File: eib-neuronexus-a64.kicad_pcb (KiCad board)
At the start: 2 copper layers, 53 x 59 mm, 5 parts, among them J1 xOLC-110-01-S-Q_1, J2 xOLC-110-01-S-Q_1, J3 Conn_02x35_Odd_Even, J4 Conn_01x02_Male

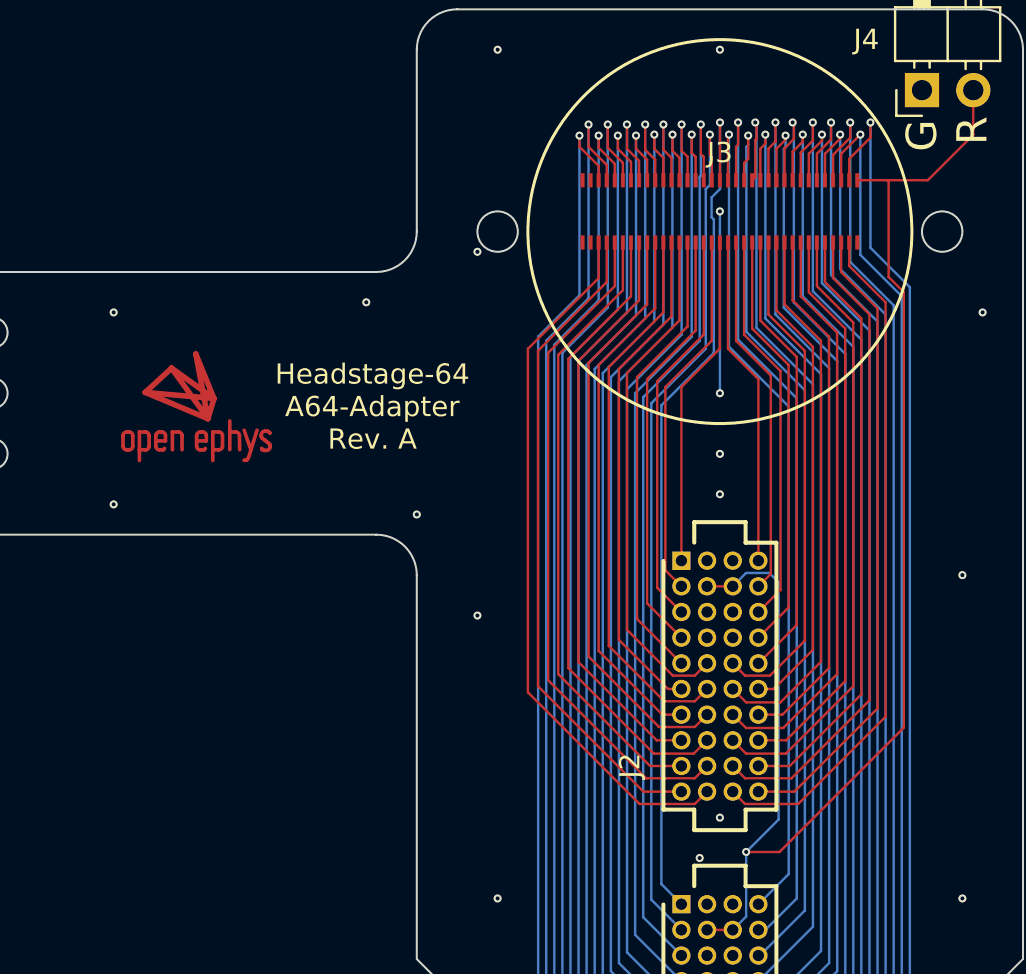
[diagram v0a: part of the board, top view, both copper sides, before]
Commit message: Revision B
- Fixed pinout to match 1.3B headstage-64
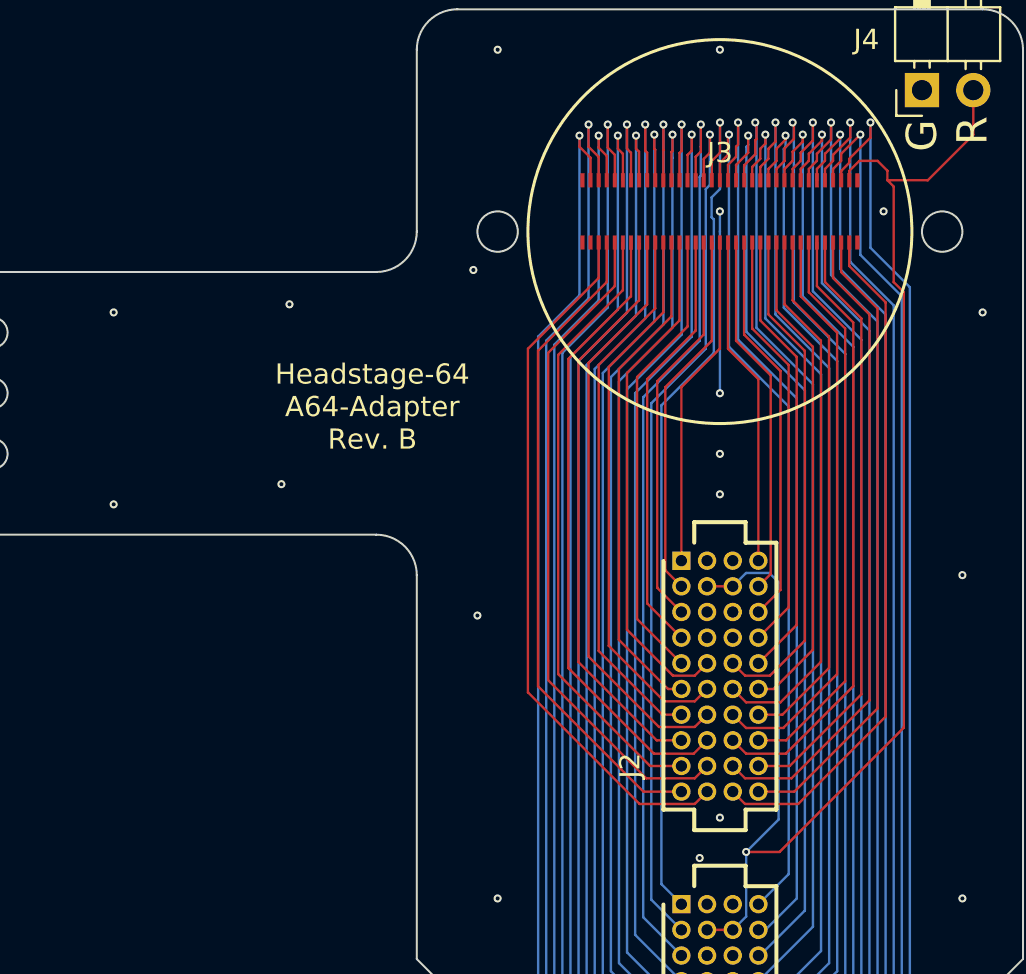
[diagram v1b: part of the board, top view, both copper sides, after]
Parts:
- removed ?: , jonnew-eagle:OE-LOGO-7X5
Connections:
- J3 pad 10: /Elec3 -> /Elec2
- J3 pad 12: /Elec4 -> /Elec3
- J3 pad 14: /Elec5 -> /Elec4
- J3 pad 16: /Elec6 -> /Elec5
- J3 pad 18: /Elec7 -> /Elec6
- J3 pad 2: /Ref -> GND
- J3 pad 20: /Elec8 -> /Elec7
- J3 pad 22: /Elec9 -> /Elec8
- J3 pad 24: /Elec10 -> /Elec9
- J3 pad 26: /Elec11 -> /Elec10
- J3 pad 28: /Elec12 -> /Elec11
- J3 pad 30: /Elec13 -> /Elec12
- J3 pad 32: /Elec14 -> /Elec13
- J3 pad 34: /Elec15 -> /Elec14
- J3 pad 36: /Elec48 -> /Elec15
- J3 pad 38: /Elec49 -> /Elec48
- J3 pad 4: /Elec0 -> /Ref
- J3 pad 40: /Elec50 -> /Elec49
- J3 pad 42: /Elec51 -> /Elec50
- J3 pad 44: /Elec52 -> /Elec51
- J3 pad 46: /Elec53 -> /Elec52
- J3 pad 48: /Elec54 -> /Elec53
- J3 pad 50: /Elec55 -> /Elec54
- J3 pad 52: /Elec56 -> /Elec55
- J3 pad 54: /Elec57 -> /Elec56
- J3 pad 56: /Elec58 -> /Elec57
- J3 pad 58: /Elec59 -> /Elec58
- J3 pad 6: /Elec1 -> /Elec0
- J3 pad 60: /Elec60 -> /Elec59
- J3 pad 62: /Elec61 -> /Elec60
- J3 pad 64: /Elec62 -> /Elec61
- J3 pad 66: /Elec63 -> /Elec62
- J3 pad 68: GND -> /Elec63
- J3 pad 8: /Elec2 -> /Elec1
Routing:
- net /Ref: track 70.1 -> 71.8 mm
- net GND: vias 19 -> 20
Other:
- board text added: "Headstage-64 A64-Adapter Rev. B"
- board text removed: "Headstage-64 A64-Adapter Rev. A"
